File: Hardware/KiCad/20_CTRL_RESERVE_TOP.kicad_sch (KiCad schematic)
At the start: 0 parts

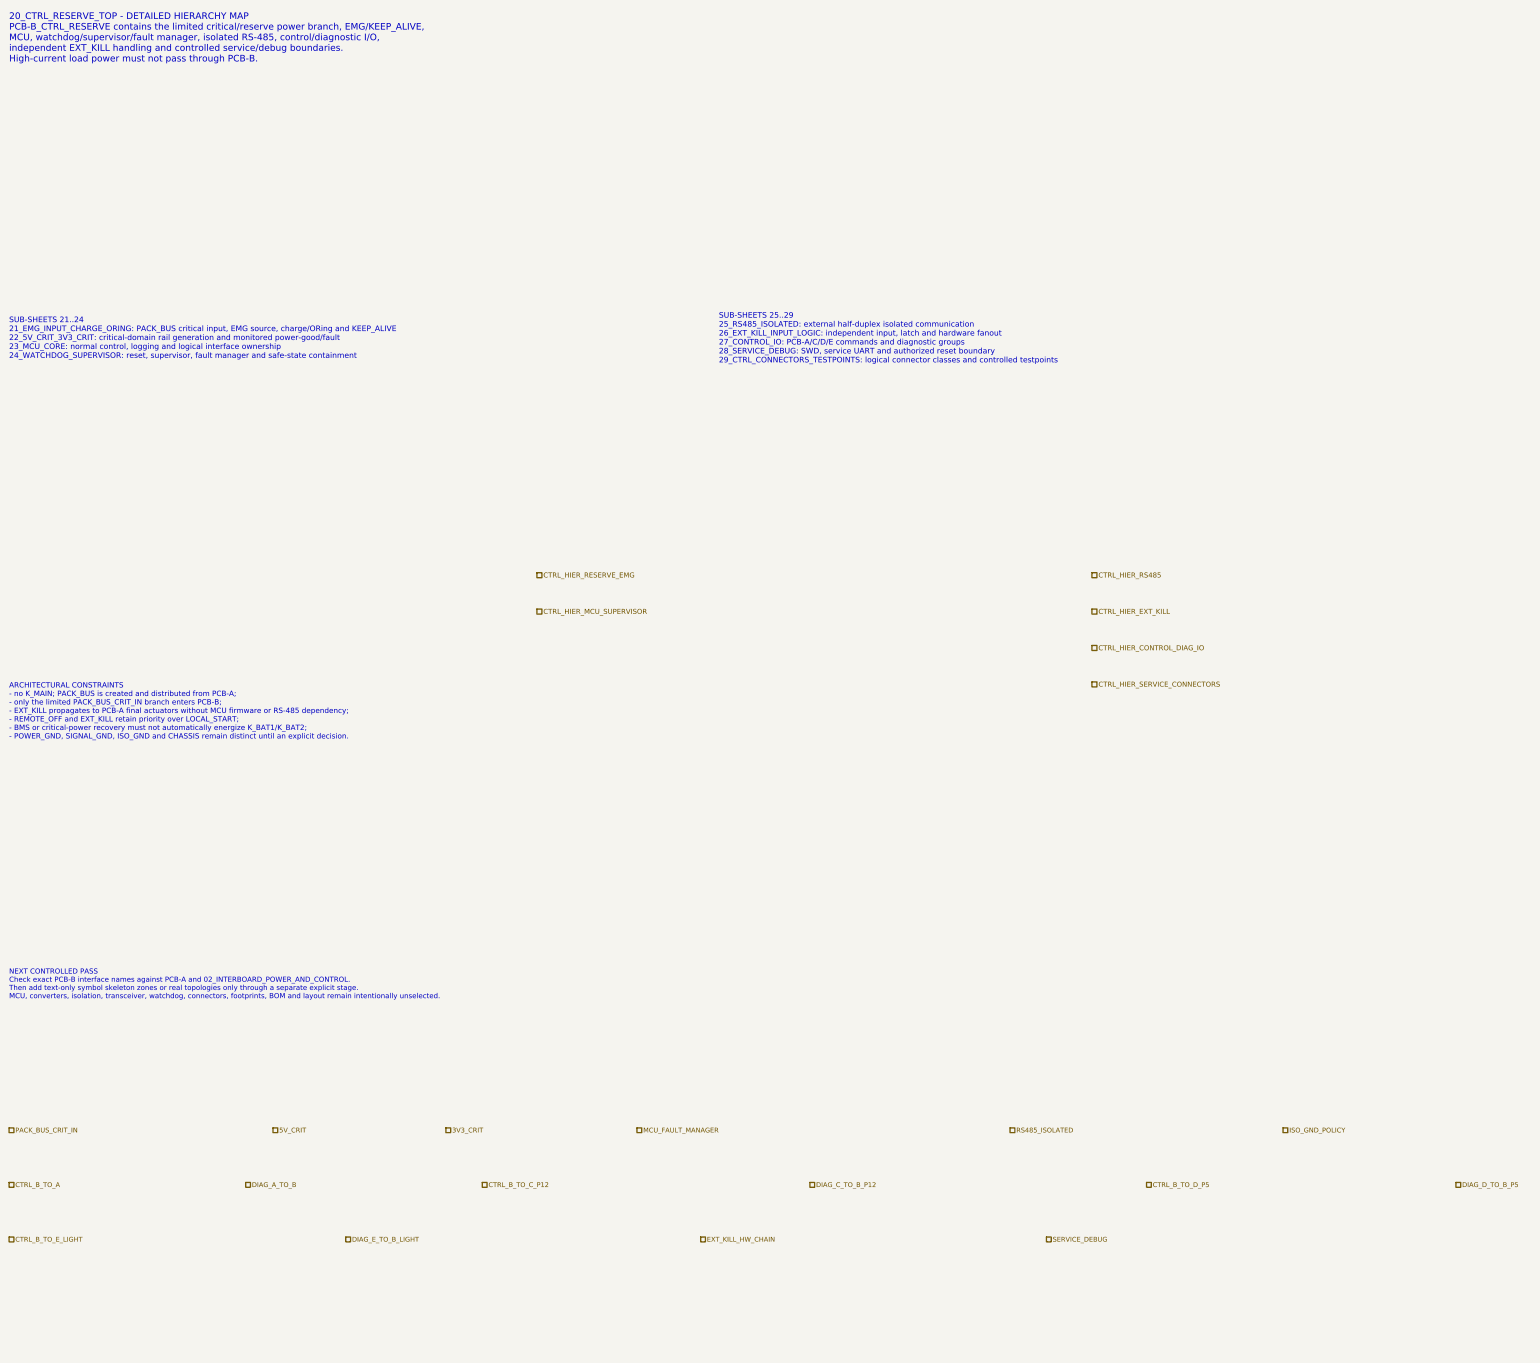
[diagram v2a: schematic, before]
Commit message: hardware: align PCB-B top boundary to V1.6 transport and ground policy
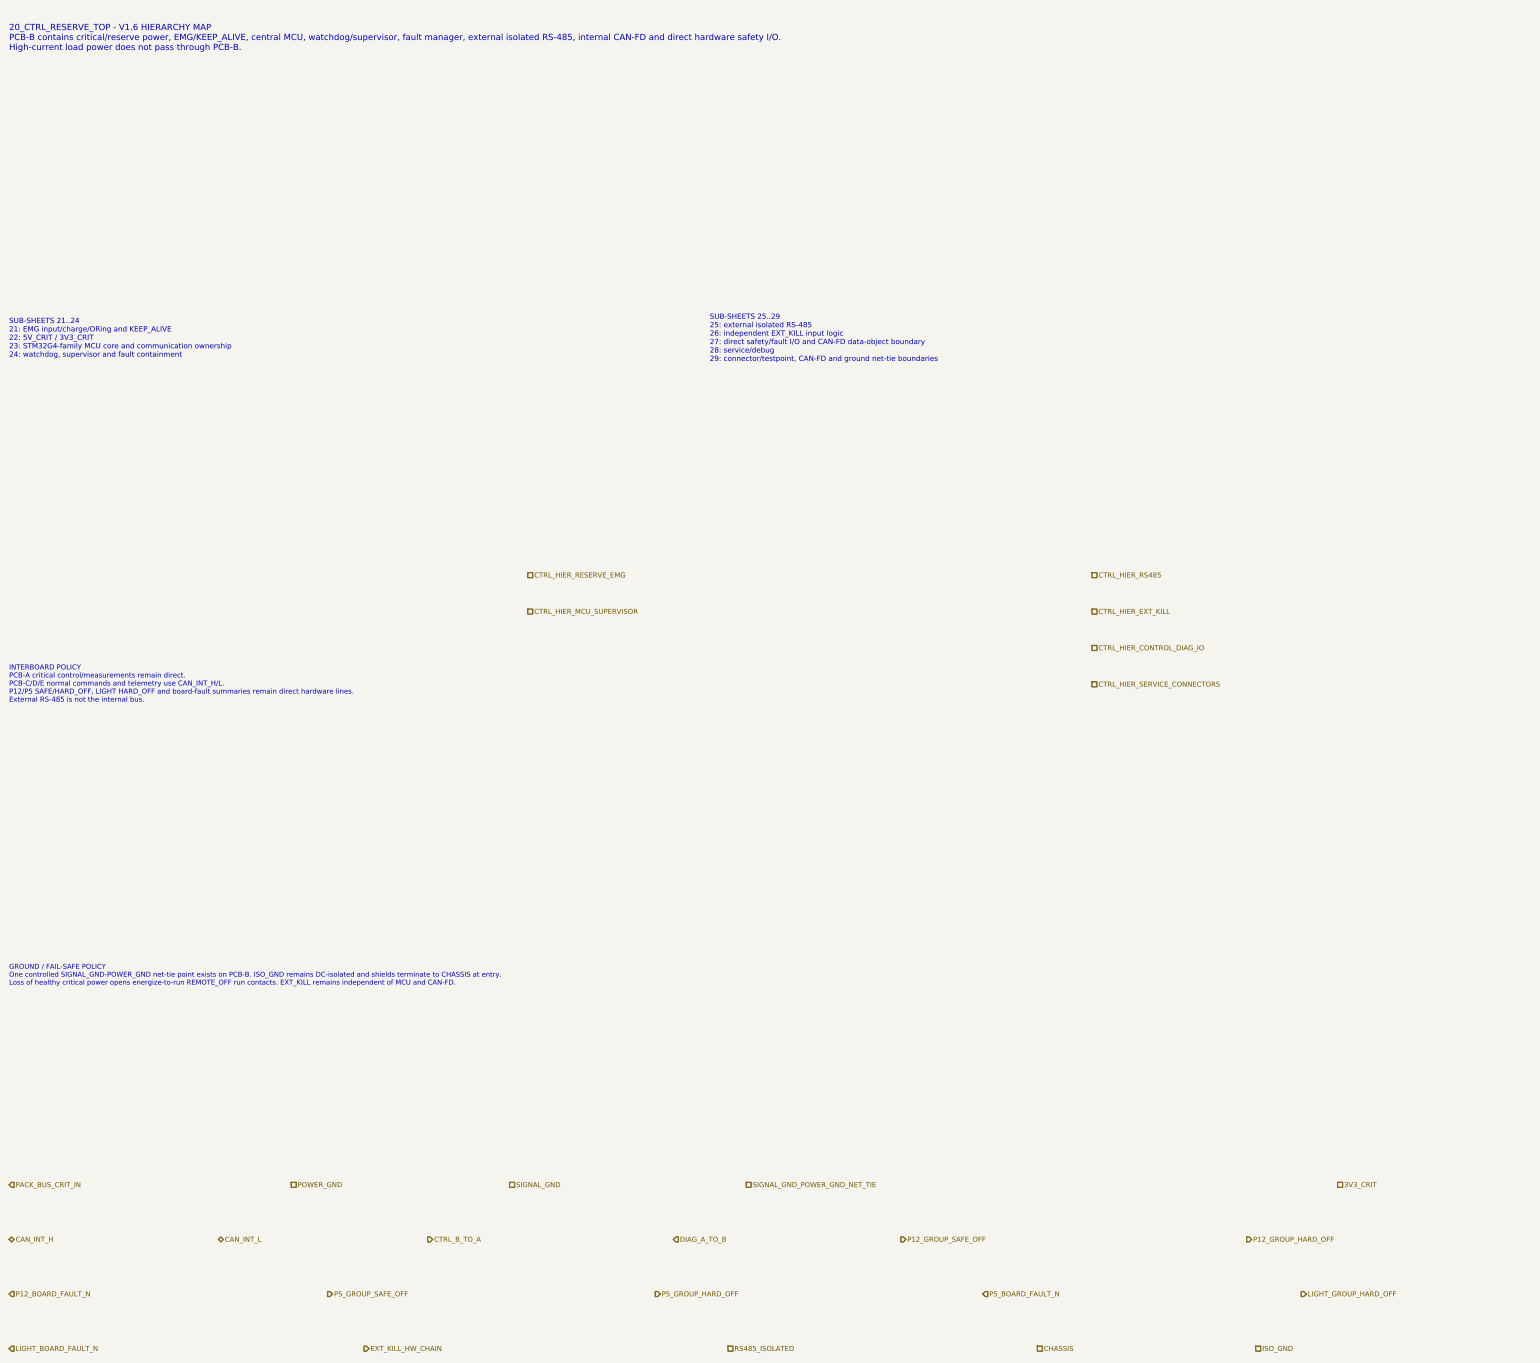
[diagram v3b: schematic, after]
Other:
- note added: "20_CTRL_RESERVE_TOP - V1.6 HIERARCHY MAP PCB-B contains critical/reserve power, EMG/KEEP_ALIVE, central MCU, watchdog/supervisor, fault manager, external isolated RS-485, internal CAN-FD and direct hardware safety I/O. High-current load power does not pass through PCB-B."
- note added: "GROUND / FAIL-SAFE POLICY One controlled SIGNAL_GND-POWER_GND net-tie point exists on PCB-B. ISO_GND remains DC-isolated and shields terminate to CHASSIS at entry. Loss of healthy critical power opens energize-to-run REMOTE_OFF run contacts. EXT_KILL remains independent of MCU and CAN-FD."
- note added: "INTERBOARD POLICY PCB-A critical control/measurements remain direct. PCB-C/D/E normal commands and telemetry use CAN_INT_H/L. P12/P5 SAFE/HARD_OFF, LIGHT HARD_OFF and board-fault summaries remain direct hardware lines. External RS-485 is not the internal bus."
- note added: "SUB-SHEETS 21..24 21: EMG input/charge/ORing and KEEP_ALIVE 22: 5V_CRIT / 3V3_CRIT 23: STM32G4-family MCU core and communication ownership 24: watchdog, supervisor and fault containment"
- note added: "SUB-SHEETS 25..29 25: external isolated RS-485 26: independent EXT_KILL input logic 27: direct safety/fault I/O and CAN-FD data-object boundary 28: service/debug 29: connector/testpoint, CAN-FD and ground net-tie boundaries"
- note removed: "20_CTRL_RESERVE_TOP - DETAILED HIERARCHY MAP PCB-B_CTRL_RESERVE contains the limited critical/reserve power branch, EMG/KEEP_ALIVE, MCU, watchdog/supervisor/fault manager, isolated RS-485, control/diagnostic I/O, independent EXT_KILL handling and controlled service/debug boundaries. High-current load power must not pass through PCB-B."
- note removed: "ARCHITECTURAL CONSTRAINTS - no K_MAIN; PACK_BUS is created and distributed from PCB-A; - only the limited PACK_BUS_CRIT_IN branch enters PCB-B; - EXT_KILL propagates to PCB-A final actuators without MCU firmware or RS-485 dependency; - REMOTE_OFF and EXT_KILL retain priority over LOCAL_START; - BMS or critical-power recovery must not automatically energize K_BAT1/K_BAT2; - POWER_GND, SIGNAL_GND, 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"
- note removed: "NEXT CONTROLLED PASS Check exact PCB-B interface names against PCB-A and 02_INTERBOARD_POWER_AND_CONTROL. Then add text-only symbol skeleton zones or real topologies only through a separate explicit stage. MCU, converters, isolation, transceiver, watchdog, connectors, footprints, BOM and layout remain intentionally unselected."
- note removed: "SUB-SHEETS 21..24 21_EMG_INPUT_CHARGE_ORING: PACK_BUS critical input, EMG source, charge/ORing and KEEP_ALIVE 22_5V_CRIT_3V3_CRIT: critical-domain rail generation and monitored power-good/fault 23_MCU_CORE: normal control, logging and logical interface ownership 24_WATCHDOG_SUPERVISOR: reset, supervisor, fault manager and safe-state containment"
- note removed: "SUB-SHEETS 25..29 25_RS485_ISOLATED: external half-duplex isolated communication 26_EXT_KILL_INPUT_LOGIC: independent input, latch and hardware fanout 27_CONTROL_IO: PCB-A/C/D/E commands and diagnostic groups 28_SERVICE_DEBUG: SWD, service UART and authorized reset boundary 29_CTRL_CONNECTORS_TESTPOINTS: logical connector classes and controlled testpoints"
